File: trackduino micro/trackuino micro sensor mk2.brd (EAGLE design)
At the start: 43.3 x 19.1 mm, 42 parts, among them IC2 74AHC1G125DBV, SW1 SPST_TACT-KMR2, U1 ATMEGA168MLF, Y1 16MHZ

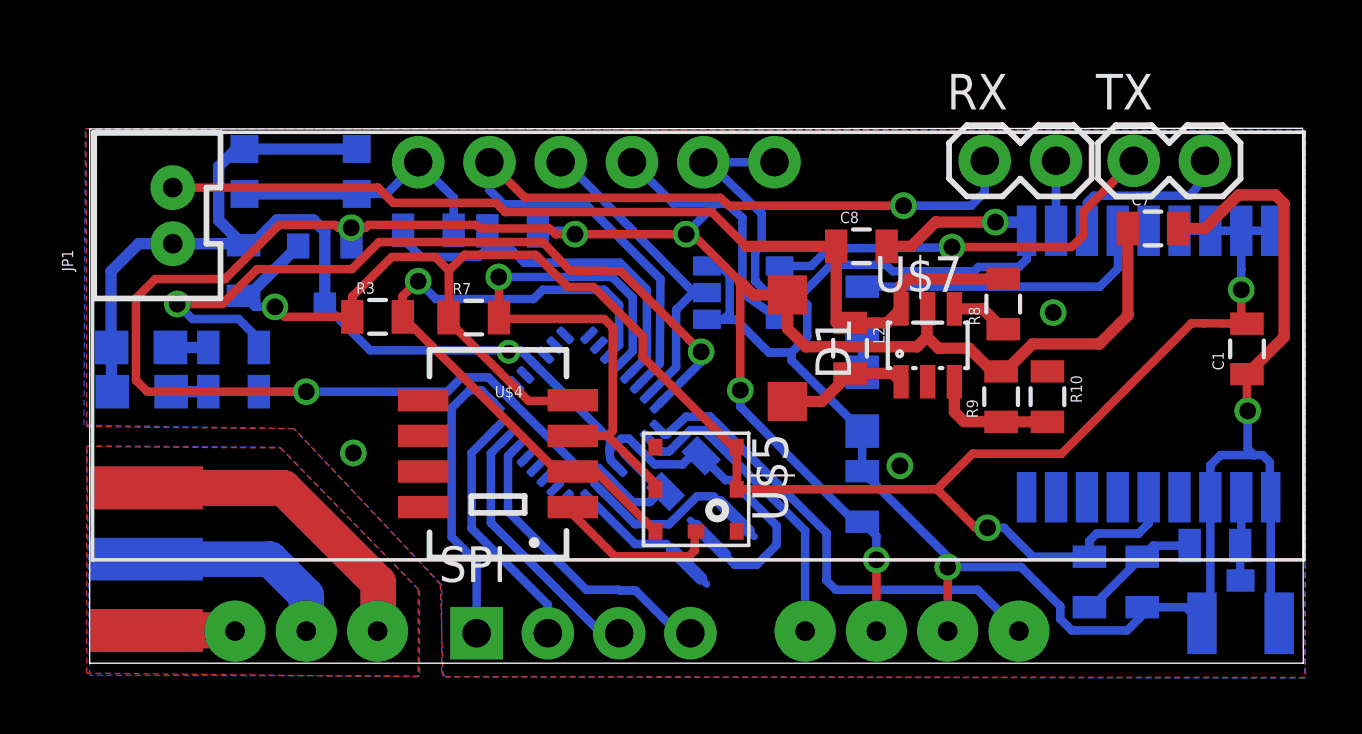
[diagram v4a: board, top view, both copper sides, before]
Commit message: boost converter fix
fixed external component placement and added some silkscreen
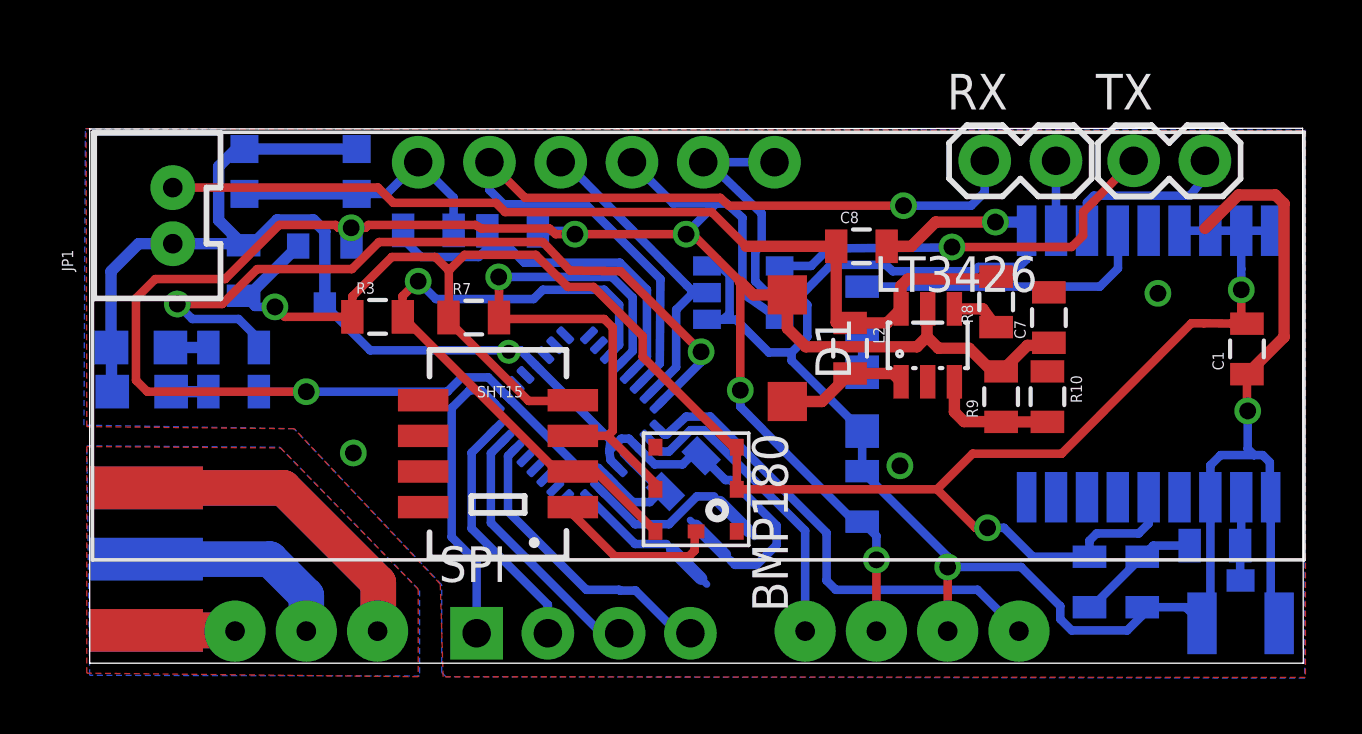
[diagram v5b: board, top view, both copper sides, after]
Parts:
- moved C7 4.88 mm to (85.6, 69.8), turned to 90 degrees
- moved R8 0.27 mm to (83.7, 70.4)
- renumbered U$3 to LM3480, U$4 to SHT15, U$5 to BMP180, U$7 to LT3426
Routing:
- net VCC: track 99.4 -> 93.1 mm
- net GND: track 167.5 -> 166.5 mm
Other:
- board text added: "SBHX TRACKOON Rev .9"
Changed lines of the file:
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@@
 <wire x1="94.6152" y1="76.571" x2="51.3842" y2="76.5456" width="0" layer="20"/>
 <wire x1="51.3842" y1="76.5456" x2="51.3842" y2="57.5056" width="0" layer="20"/>
+<text x="61.5696" y="59.9948" size="0.8128" layer="26" rot="MR0">SBHX TRACKOON
+Rev .9</text>
 </plain>
 <attributes>
@@
 <element name="IC2" library="74xx-little-us" package="SOT23-5" value="74AHC1G125DBV" x="74.676" y="70.7136" rot="MR90"/>
 <element name="U$2" library="Ava" package="RADIOMETRIX-HX1" value="RADIOMETRIX-HX1" x="73.0758" y="68.8086"/>
-<element name="U$3" library="SparkFun-PowerIC" package="SOT23-3" value="LM3480IM4" x="59.7662" y="71.374" rot="MR180"/>
+<element name="LM3480" library="SparkFun-PowerIC" package="SOT23-3" value="LM3480IM4" x="59.7662" y="71.374" rot="MR180"/>
 <element name="U1" library="SparkFun-DigitalIC" package="MLF32" value="ATMEGA168MLF" x="68.7578" y="66.294" rot="MR45"/>
 <element name="JP1" library="SparkFun-Connectors" package="JST-2-PTH-VERT" value="M02JST-PTH-VERT" x="53.7972" y="73.4568" rot="R90"/>
@@
 <element name="C6" library="SparkFun-Capacitors" package="0805" value="47pf" x="88.9" y="60.4012" rot="MR270"/>
 <element name="RX" library="SparkFun-Connectors" package="1X02" value="RX" x="83.2866" y="75.4126"/>
-<element name="U$4" library="SparkFun-Sensors" package="SHT1X" value="SHT1XSMD" x="65.9384" y="64.9732" rot="R180"/>
-<element name="U$5" library="SparkFun-Sensors" package="BMP180" value="BMP180" x="72.9996" y="63.7032" rot="R270"/>
+<element name="SHT15" library="SparkFun-Sensors" package="SHT1X" value="SHT1XSMD" x="65.9384" y="64.9732" rot="R180"/>
+<element name="BMP180" library="SparkFun-Sensors" package="BMP180" value="BMP180" x="72.9996" y="63.7032" rot="R270"/>
 <element name="R3" library="SparkFun-Resistors" package="0805" value="" x="61.6458" y="69.85"/>
 <element name="R7" library="SparkFun-Resistors" package="0805" value="" x="65.0748" y="69.8246"/>
-<element name="U$7" library="adafruit" package="SOT23-6" value="LT3426" x="81.2546" y="68.834"/>
+<element name="LT3426" library="adafruit" package="SOT23-6" value="LT3426" x="81.2546" y="68.834"/>
 <element name="D1" library="diode" package="SOD123" value="MBR120VLSFT1" x="76.2508" y="68.7324" rot="R270"/>
 <element name="L2" library="SparkFun-Passives" package="0805" value="2.2uh" x="78.486" y="68.7324" rot="R270"/>
-<element name="R8" library="SparkFun-Resistors" package="0805" value="1m" x="83.947" y="70.3072" rot="R90"/>
+<element name="R8" library="SparkFun-Resistors" package="0805" value="1m" x="83.693" y="70.3834" rot="R90"/>
 <element name="R9" library="SparkFun-Resistors" package="0805" value="95.3k" x="83.8708" y="67.0052" rot="R90"/>
 <element name="R10" library="SparkFun-Resistors" package="0805" value="30.9k" x="85.5218" y="67.0052" rot="R270"/>
-<element name="C7" library="SparkFun-Capacitors" package="0805" value="22uf" x="89.281" y="72.9996"/>
+<element name="C7" library="SparkFun-Capacitors" package="0805" value="22uf" x="85.5726" y="69.8246" rot="R90"/>
 <element name="C8" library="SparkFun-Capacitors" package="0805" value="10uf" x="78.8924" y="72.3646"/>
 </elements>
@@
 <contactref element="SW1" pad="4"/>
 <contactref element="C2" pad="1"/>
-<contactref element="U$3" pad="3"/>
+<contactref element="LM3480" pad="3"/>
 <contactref element="C6" pad="2"/>
 <contactref element="FTDI" pad="5"/>
-<contactref element="U$4" pad="1"/>
-<contactref element="U$5" pad="7"/>
+<contactref element="SHT15" pad="1"/>
+<contactref element="BMP180" pad="7"/>
 <wire x1="60.9026" y1="75.8316" x2="56.9026" y2="75.8316" width="0.4064" layer="16"/>
 <wire x1="54.3472" y1="72.4568" x2="53.1274" y2="72.4568" width="0.4064" layer="16"/>
@@
 <via x="80.264" y="64.5414" extent="1-16" drill="0.6" shape="square"/>
 <wire x1="53.2892" y1="58.674" x2="56.5912" y2="58.674" width="1.27" layer="1"/>
-<contactref element="U$7" pad="2"/>
+<contactref element="LT3426" pad="2"/>
 <contactref element="R10" pad="1"/>
 <contactref element="C8" pad="2"/>
@@
 <wire x1="83.6676" y1="73.2282" x2="84.5732" y2="73.2282" width="0.4064" layer="16"/>
 <wire x1="84.5732" y1="73.2282" x2="84.7794" y2="72.9204" width="0.4064" layer="16"/>
-<wire x1="90.181" y1="72.9996" x2="91.1352" y2="72.9996" width="0.4064" layer="1"/>
 <wire x1="91.1352" y1="72.9996" x2="92.329" y2="74.1934" width="0.4064" layer="1"/>
 <wire x1="92.329" y1="74.1934" x2="93.6498" y2="74.1934" width="0.4064" layer="1"/>
@@
 <wire x1="93.9546" y1="73.8886" x2="93.9546" y2="69.1278" width="0.4064" layer="1"/>
 <wire x1="93.9546" y1="69.1278" x2="92.6338" y2="67.807" width="0.4064" layer="1"/>
-<via x="85.725" y="70.0024" extent="1-16" drill="0.6" shape="square"/>
+<via x="89.4588" y="70.6882" extent="1-16" drill="0.6" shape="square"/>
 <via x="60.7822" y="64.9986" extent="1-16" drill="0.6" shape="square"/>
 <via x="66.3194" y="68.6054" extent="1-16" drill="0.5"/>
@@
 <signal name="VCC">
 <contactref element="IC2" pad="5"/>
-<contactref element="U$3" pad="2"/>
+<contactref element="LM3480" pad="2"/>
 <contactref element="U$2" pad="VCC"/>
 <contactref element="C3" pad="2"/>
@@
 <wire x1="60.1472" y1="73.1266" x2="60.2488" y2="73.025" width="0.3048" layer="1"/>
 <wire x1="60.2488" y1="73.025" x2="60.706" y2="73.025" width="0.3048" layer="1"/>
-<contactref element="U$7" pad="5"/>
+<contactref element="LT3426" pad="5"/>
 <contactref element="D1" pad="C"/>
 <contactref element="R9" pad="2"/>
 <contactref element="C7" pad="1"/>
-<wire x1="88.3666" y1="72.9852" x2="88.381" y2="72.9996" width="0.4064" layer="1"/>
 <wire x1="76.2508" y1="70.6324" x2="75.0366" y2="70.6324" width="0.4064" layer="1"/>
 <wire x1="75.0366" y1="70.6324" x2="74.5744" y2="71.0946" width="0.4064" layer="1"/>
@@
 <wire x1="82.7278" y1="68.7324" x2="81.6356" y2="68.7324" width="0.4064" layer="1"/>
 <wire x1="81.6356" y1="68.7324" x2="81.2292" y2="69.1388" width="0.4064" layer="1"/>
-<wire x1="83.8708" y1="67.9052" x2="84.0088" y2="67.9052" width="0.4064" layer="1"/>
-<wire x1="84.0088" y1="67.9052" x2="84.9884" y2="68.8848" width="0.4064" layer="1"/>
-<wire x1="84.9884" y1="68.8848" x2="87.376" y2="68.8848" width="0.4064" layer="1"/>
-<wire x1="87.376" y1="68.8848" x2="88.392" y2="69.9008" width="0.4064" layer="1"/>
-<wire x1="88.392" y1="69.9008" x2="88.392" y2="72.9886" width="0.4064" layer="1"/>
-<wire x1="88.392" y1="72.9886" x2="88.381" y2="72.9996" width="0.4064" layer="1"/>
+<wire x1="83.8708" y1="67.9052" x2="83.8818" y2="67.9052" width="0.4064" layer="1"/>
+<wire x1="83.8818" y1="67.9052" x2="84.8106" y2="68.834" width="0.4064" layer="1"/>
+<wire x1="84.8106" y1="68.834" x2="85.5582" y2="68.834" width="0.4064" layer="1"/>
+<wire x1="85.5582" y1="68.834" x2="85.5726" y2="68.9246" width="0.4064" layer="1"/>
 </signal>
 <signal name="D3">
@@
 </signal>
 <signal name="3V">
-<contactref element="U$3" pad="1"/>
+<contactref element="LM3480" pad="1"/>
 <contactref element="C2" pad="2"/>
 <contactref element="C1" pad="2"/>
@@
 <contactref element="U$1" pad="14_VCC_RF"/>
 <contactref element="R2" pad="2"/>
-<contactref element="U$5" pad="2"/>
-<contactref element="U$5" pad="3"/>
-<contactref element="U$4" pad="4"/>
+<contactref element="BMP180" pad="2"/>
+<contactref element="BMP180" pad="3"/>
+<contactref element="SHT15" pad="4"/>
 <contactref element="R3" pad="1"/>
 <contactref element="R7" pad="1"/>
@@
 <signal name="SDA">
 <contactref element="U1" pad="27"/>
-<contactref element="U$4" pad="2"/>
-<contactref element="U$5" pad="6"/>
+<contactref element="SHT15" pad="2"/>
+<contactref element="BMP180" pad="6"/>
 <contactref element="R3" pad="2"/>
 <wire x1="69.889171875" y1="68.486028125" x2="70.2564" y2="68.85325625" width="0.3048" layer="16"/>
@@
 <signal name="SCL">
 <contactref element="U1" pad="28"/>
-<contactref element="U$4" pad="3"/>
-<contactref element="U$5" pad="5"/>
+<contactref element="SHT15" pad="3"/>
+<contactref element="BMP180" pad="5"/>
 <contactref element="R7" pad="2"/>
 <wire x1="70.242725" y1="68.132475" x2="70.739" y2="68.62875" width="0.3048" layer="16"/>
@@
 <wire x1="66.1924" y1="73.5838" x2="73.5584" y2="73.5838" width="0.3048" layer="1"/>
 <wire x1="73.5584" y1="73.5838" x2="74.7776" y2="72.3646" width="0.3048" layer="1"/>
-<contactref element="U$7" pad="6"/>
+<contactref element="LT3426" pad="6"/>
 <contactref element="L2" pad="1"/>
 <contactref element="R8" pad="2"/>
@@
 <wire x1="80.3046" y1="70.9574" x2="80.5434" y2="71.1962" width="0.4064" layer="1"/>
 <wire x1="80.5434" y1="71.1962" x2="83.936" y2="71.1962" width="0.4064" layer="1"/>
-<wire x1="83.936" y1="71.1962" x2="83.947" y2="71.2072" width="0.4064" layer="1"/>
+<wire x1="83.936" y1="71.1962" x2="83.693" y2="71.2834" width="0.4064" layer="1"/>
 </signal>
 <signal name="N$7">
@@
 </signal>
 <signal name="N$9">
-<contactref element="U$7" pad="1"/>
+<contactref element="LT3426" pad="1"/>
 <contactref element="D1" pad="A"/>
 <contactref element="L2" pad="2"/>
@@
 </signal>
 <signal name="N$12">
-<contactref element="U$7" pad="4"/>
+<contactref element="LT3426" pad="4"/>
 <contactref element="R8" pad="1"/>
 <wire x1="82.2046" y1="70.134" x2="83.2202" y2="70.134" width="0.4064" layer="1"/>
-<wire x1="83.2202" y1="70.134" x2="83.947" y2="69.4072" width="0.4064" layer="1"/>
+<wire x1="83.2202" y1="70.134" x2="83.693" y2="69.4834" width="0.4064" layer="1"/>
 </signal>
 <signal name="N$13">
 <contactref element="R9" pad="1"/>
 <contactref element="R10" pad="2"/>
-<contactref element="U$7" pad="3"/>
+<contactref element="LT3426" pad="3"/>
 <wire x1="83.8708" y1="66.1052" x2="85.5218" y2="66.1052" width="0.4064" layer="1"/>
 <wire x1="82.2046" y1="67.534" x2="82.2046" y2="66.4616" width="0.4064" layer="1"/>
@@
 </board>
 </drawing>
+<compatibility>
+<note version="6.3" minversion="6.2.2" severity="warning">
+Since Version 6.2.2 text objects can contain more than one line,
+which will not be processed correctly with this version.
+</note>
+</compatibility>
 </eagle>

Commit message: added part values
added part values to the schematic.
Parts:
- C1, C2, C3, C4, C5: value (none) -> .1uf
- R1: value (none) -> 100ohm
- R3, R7: value (none) -> 4.7k
- R4, R6: value (none) -> 330ohm
- R5: value (none) -> 10k
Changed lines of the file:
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@@
 <element name="JP1" library="SparkFun-Connectors" package="JST-2-PTH-VERT" value="M02JST-PTH-VERT" x="53.7972" y="73.4568" rot="R90"/>
 <element name="J$1" library="SparkFun-Connectors" package="SMA-EDGE" value="SMA_EDGE" x="53.3908" y="58.674" rot="MR90"/>
-<element name="R1" library="SparkFun-Resistors" package="0805" value="" x="78.9178" y="70.0278" rot="MR270"/>
+<element name="R1" library="SparkFun-Resistors" package="0805" value="100ohm" x="78.9178" y="70.0278" rot="MR270"/>
 <element name="LED1" library="adafruit" package="CHIP-LED0805" value="" x="78.9178" y="66.8274" rot="MR180"/>
-<element name="C1" library="SparkFun-Capacitors" package="0805" value="" x="92.6338" y="68.707" rot="R90"/>
-<element name="C2" library="SparkFun-Capacitors" package="0805" value="" x="56.8706" y="71.501" rot="MR270"/>
-<element name="C3" library="SparkFun-Capacitors" package="0805" value="" x="72.5424" y="64.262" rot="MR315"/>
-<element name="C4" library="SparkFun-Capacitors" package="0805" value="" x="78.9178" y="63.4492" rot="MR270"/>
+<element name="C1" library="SparkFun-Capacitors" package="0805" value=".1uf" x="92.6338" y="68.707" rot="R90"/>
+<element name="C2" library="SparkFun-Capacitors" package="0805" value=".1uf" x="56.8706" y="71.501" rot="MR270"/>
+<element name="C3" library="SparkFun-Capacitors" package="0805" value=".1uf" x="72.5424" y="64.262" rot="MR315"/>
+<element name="C4" library="SparkFun-Capacitors" package="0805" value=".1uf" x="78.9178" y="63.4492" rot="MR270"/>
 <element name="LED3" library="adafruit" package="CHIP-LED0805" value="" x="53.2384" y="67.183" rot="MR270"/>
-<element name="R4" library="SparkFun-Resistors" package="0805" value="" x="56.515" y="67.183" rot="MR180"/>
+<element name="R4" library="SparkFun-Resistors" package="0805" value="330ohm" x="56.515" y="67.183" rot="MR180"/>
 <element name="FTDI" library="SparkFun-Connectors" package="1X06_NO_SILK" value="" x="63.0936" y="75.3618" rot="MR180">
 <attribute name="PROD_ID" value="CONN-08437" x="63.0936" y="75.3618" size="1.778" layer="28" rot="MR180" display="off"/>
 </element>
-<element name="R5" library="SparkFun-Resistors" package="0805" value="" x="66.461275" y="72.912878125" rot="MR180"/>
-<element name="C5" library="SparkFun-Capacitors" package="0805" value="" x="63.455359375" y="72.933175" rot="MR0"/>
+<element name="R5" library="SparkFun-Resistors" package="0805" value="10k" x="66.461275" y="72.912878125" rot="MR180"/>
+<element name="C5" library="SparkFun-Capacitors" package="0805" value=".1uf" x="63.455359375" y="72.933175" rot="MR0"/>
 <element name="TX" library="SparkFun-Connectors" package="1X02" value="TX" x="88.5952" y="75.4126"/>
 <element name="SPI" library="SparkFun-Connectors" package="1X04_NO_SILK" value="" x="65.1764" y="58.5724"/>
 <element name="FRAME1" library="SparkFun-Aesthetics" package="CREATIVE_COMMONS" value="FRAME-LETTER" x="65.7606" y="49.3522"/>
 <element name="LED4" library="adafruit" package="CHIP-LED0805" value="" x="53.213" y="68.7578" rot="MR270"/>
-<element name="R6" library="SparkFun-Resistors" package="0805" value="" x="56.515" y="68.7578" rot="MR180"/>
+<element name="R6" library="SparkFun-Resistors" package="0805" value="330ohm" x="56.515" y="68.7578" rot="MR180"/>
 <element name="Y1" library="SparkFun-FreqCtrl" package="RESONATOR-SMD" value="16MHZ" x="73.51015" y="61.884171875" rot="MR315">
 <attribute name="PROD_ID" value="XTAL-08900" x="73.51015" y="61.884171875" size="1.778" layer="28" rot="MR315" display="off"/>
@@
 <element name="SHT15" library="SparkFun-Sensors" package="SHT1X" value="SHT1XSMD" x="65.9384" y="64.9732" rot="R180"/>
 <element name="BMP180" library="SparkFun-Sensors" package="BMP180" value="BMP180" x="72.9996" y="63.7032" rot="R270"/>
-<element name="R3" library="SparkFun-Resistors" package="0805" value="" x="61.6458" y="69.85"/>
-<element name="R7" library="SparkFun-Resistors" package="0805" value="" x="65.0748" y="69.8246"/>
+<element name="R3" library="SparkFun-Resistors" package="0805" value="4.7k" x="61.6458" y="69.85"/>
+<element name="R7" library="SparkFun-Resistors" package="0805" value="4.7k" x="65.0748" y="69.8246"/>
 <element name="LT3426" library="adafruit" package="SOT23-6" value="LT3426" x="81.2546" y="68.834"/>
 <element name="D1" library="diode" package="SOD123" value="MBR120VLSFT1" x="76.2508" y="68.7324" rot="R270"/>
